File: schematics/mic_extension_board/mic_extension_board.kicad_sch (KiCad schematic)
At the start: 75 parts, among them J1 XLR3, J10 Conn_01x01_Male, J2 Conn_01x02_Male, J3 Aux In, J4 I2C Bus, J5 6Pin ISP, J6 Input/Output, J7 XLR3, J8 XLR3, J9 Conn_01x03_Female, SW1 Stompbutton 1, SW2 Stompbutton 2, SW3 Stompbutton 3, U1 TL074, U10 LM4881M/NOPB, U2 TL072, U3 APE8865N-33-HF-3, U4 NE5534, U5 ATmega88A-A, U6 24LC128, U7 MC78M05_TO252, U8 MC79M08_TO252

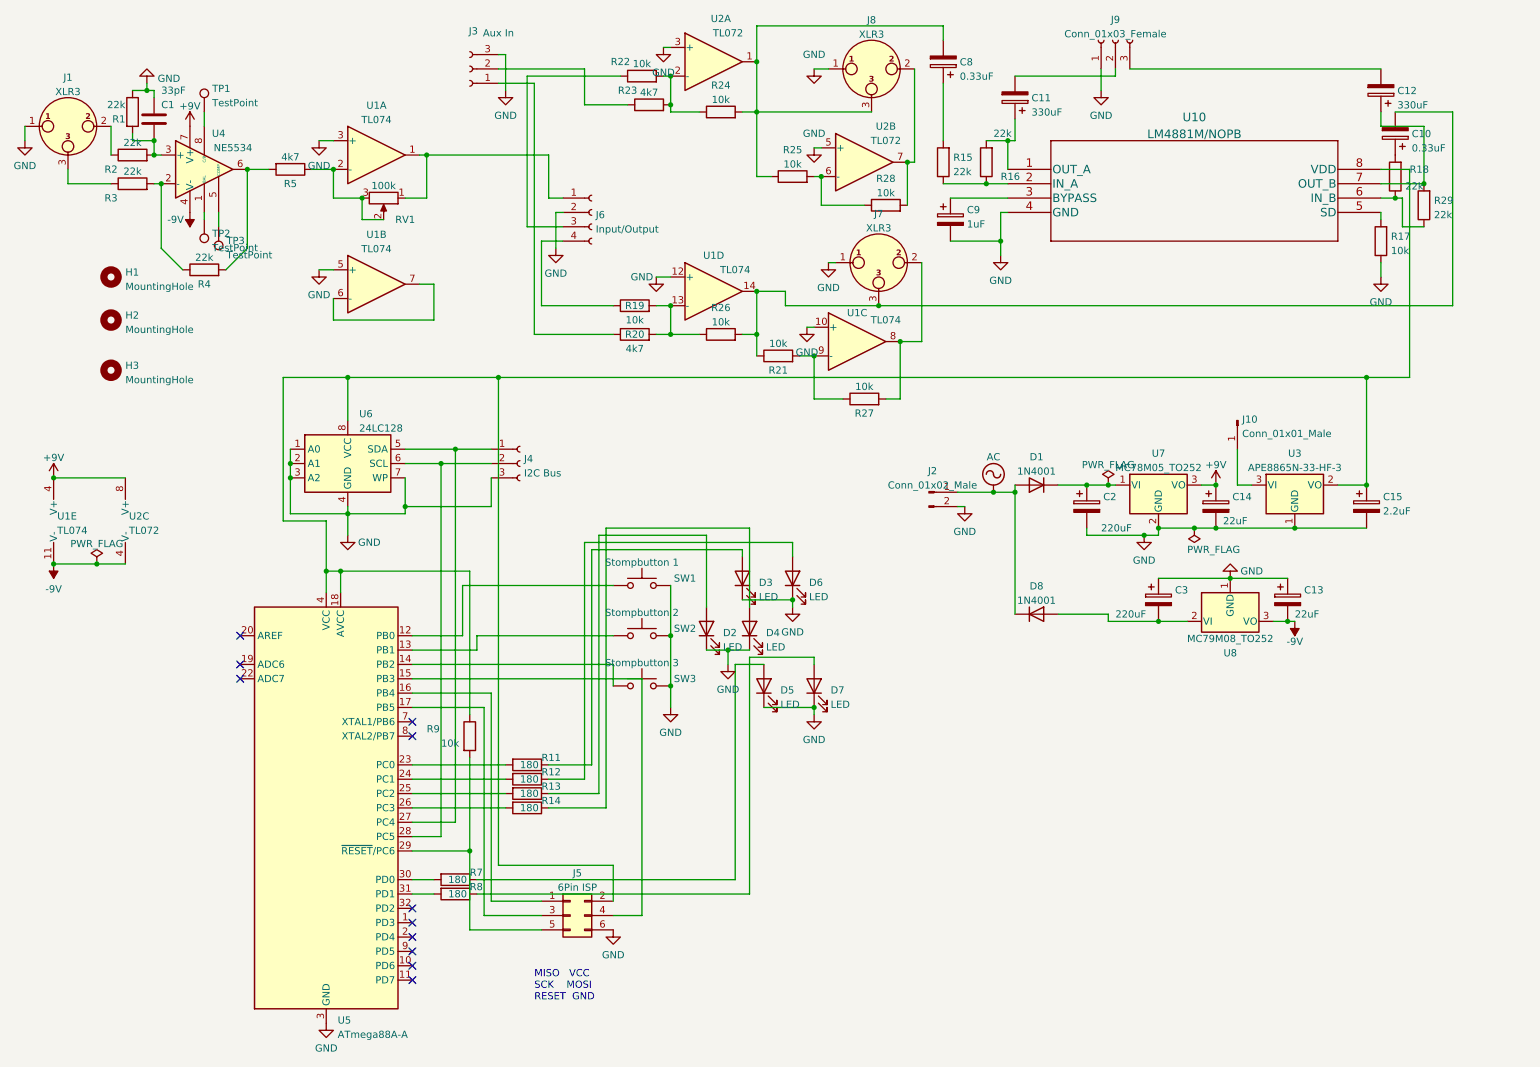
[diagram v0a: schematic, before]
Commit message: modified extension board schematic
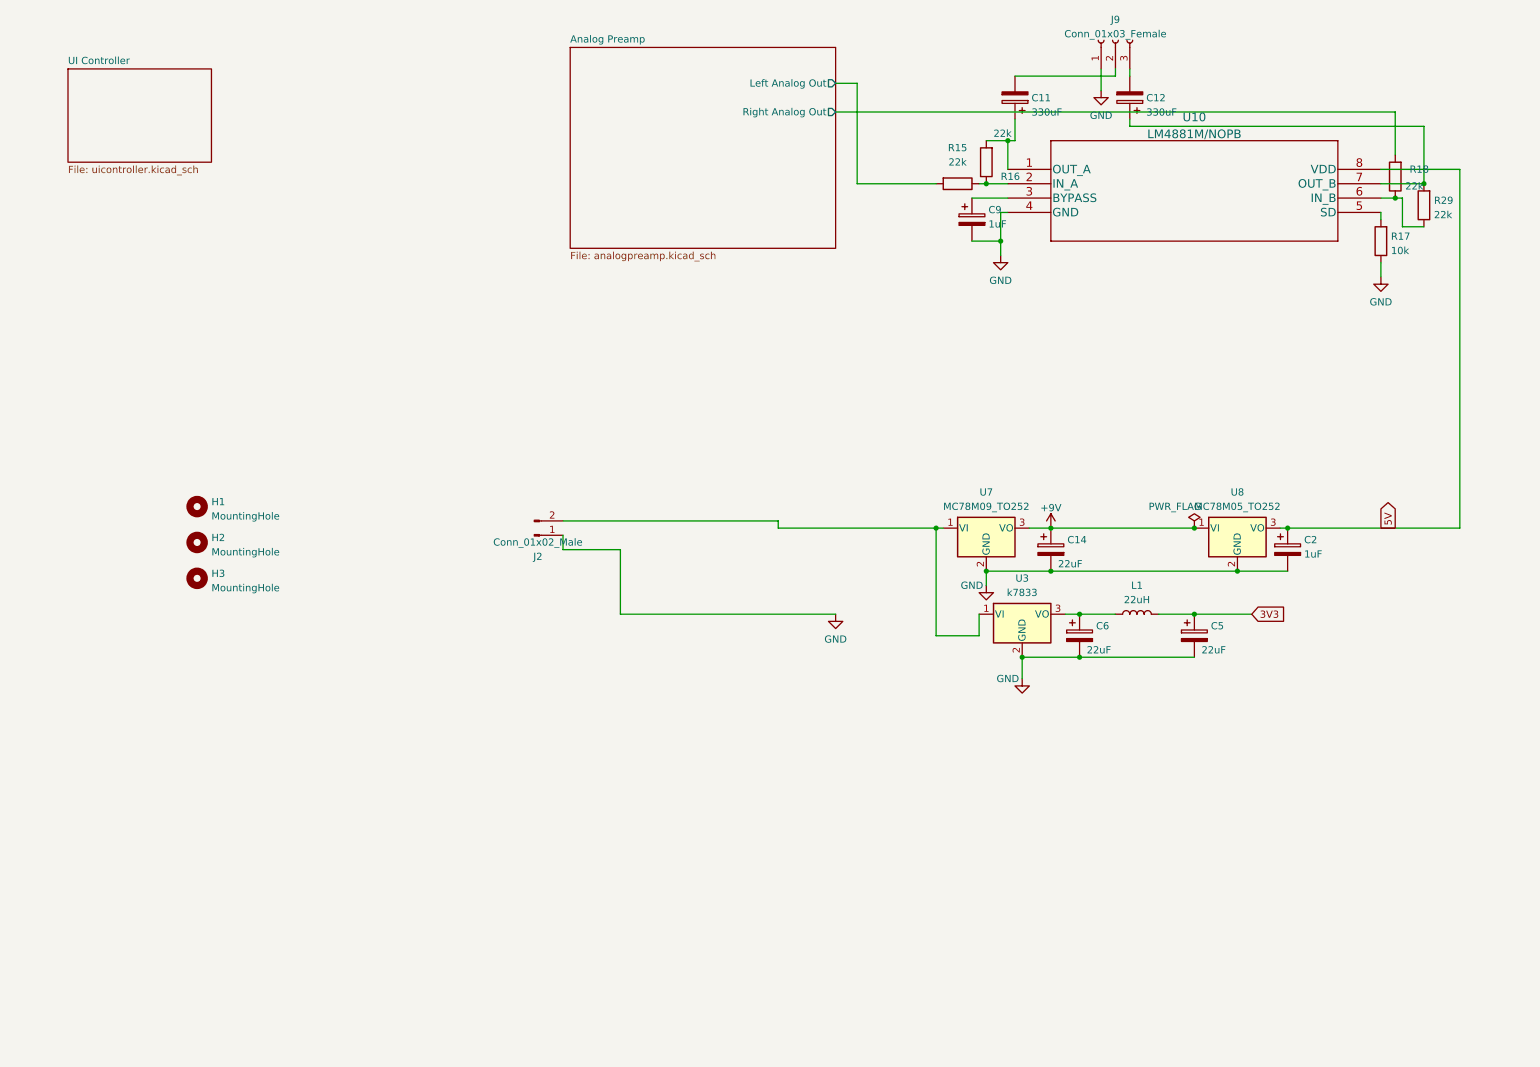
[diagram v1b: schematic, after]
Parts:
- removed C1: 33pF, Capacitor_SMD:C_0603_1608Metric_Pad1.08x0.95mm_HandSolder, symbol Device:C
- removed C10, C8: 0.33uF, Capacitor_SMD:CP_Elec_4x4.5, symbol Device:C_Polarized
- removed C13: 22uF, Capacitor_SMD:CP_Elec_4x4.5, symbol Device:C_Polarized
- removed C15: 2.2uF, Capacitor_SMD:CP_Elec_4x4.5, symbol Device:C_Polarized
- removed C3: 220uF, Capacitor_SMD:CP_Elec_6.3x7.7, symbol Device:C_Polarized
- removed D1, D8: 1N4001, Diode_THT:D_DO-41_SOD81_P10.16mm_Horizontal, symbol Diode:1N4001
- removed D2, D3, D4, D5, D6, D7: LED, Connector_PinHeader_2.54mm:PinHeader_1x02_P2.54mm_Vertical, symbol Device:LED
- removed J1, J7, J8: XLR3, Connector_PinHeader_2.54mm:PinHeader_1x03_P2.54mm_Vertical, symbol Connector:XLR3
- removed J10: Conn_01x01_Male, Connector_PinHeader_2.54mm:PinHeader_1x01_P2.54mm_Vertical, symbol Connector:Conn_01x01_Male
- removed J3: Aux In, Connector_PinHeader_2.54mm:PinHeader_1x03_P2.54mm_Vertical, symbol Connector:Conn_01x03_Female
- removed J4: I2C Bus, Connector_PinHeader_2.54mm:PinHeader_1x03_P2.54mm_Vertical, symbol Connector:Conn_01x03_Female
- removed J5: 6Pin ISP, Connector_PinHeader_2.54mm:PinHeader_2x03_P2.54mm_Vertical, symbol Connector_Generic:Conn_02x03_Odd_Even
- removed J6: Input/Output, Connector_PinHeader_2.54mm:PinHeader_1x04_P2.54mm_Vertical, symbol Connector:Conn_01x04_Female
- removed R1, R2, R3, R4: 22k, Resistor_SMD:R_0603_1608Metric_Pad0.98x0.95mm_HandSolder, symbol Device:R
- removed R11, R12, R13, R14, R7, R8: 180, Resistor_SMD:R_0603_1608Metric_Pad0.98x0.95mm_HandSolder, symbol Device:R
- removed R19, R21, R22, R24, R25, R26, R27, R28, R9: 10k, Resistor_SMD:R_0603_1608Metric_Pad0.98x0.95mm_HandSolder, symbol Device:R
- removed R20, R23, R5: 4k7, Resistor_SMD:R_0603_1608Metric_Pad0.98x0.95mm_HandSolder, symbol Device:R
- removed RV1: 100k, Connector_PinHeader_2.54mm:PinHeader_1x03_P2.54mm_Vertical, symbol Device:R_Potentiometer
- removed SW1: Stompbutton 1, Connector_PinHeader_2.54mm:PinHeader_1x02_P2.54mm_Vertical, symbol Switch:SW_Push
- removed SW2: Stompbutton 2, Connector_PinHeader_2.54mm:PinHeader_1x02_P2.54mm_Vertical, symbol Switch:SW_Push
- removed SW3: Stompbutton 3, Connector_PinHeader_2.54mm:PinHeader_1x02_P2.54mm_Vertical, symbol Switch:SW_Push
- removed TP1, TP2, TP3: TestPoint, TestPoint:TestPoint_Pad_D1.5mm, symbol Connector:TestPoint
- removed U1: TL074, Package_SO:SOIC-14_3.9x8.7mm_P1.27mm, symbol Amplifier_Operational:TL074
- removed U2: TL072, Package_SO:SOIC-8_3.9x4.9mm_P1.27mm, symbol Amplifier_Operational:TL072
- removed U3: APE8865N-33-HF-3, Package_TO_SOT_SMD:SOT-23, symbol Regulator_Linear:APE8865N-33-HF-3
- removed U4: NE5534, Package_SO:SOIC-8_3.9x4.9mm_P1.27mm, symbol Amplifier_Operational:NE5534
- removed U5: ATmega88A-A, Package_QFP:TQFP-32_7x7mm_P0.8mm, symbol MCU_Microchip_ATmega:ATmega88A-A
- removed U6: 24LC128, Package_SO:SOIC-8_3.9x4.9mm_P1.27mm, symbol Memory_EEPROM:24LC128
- removed U8: MC79M08_TO252, Package_TO_SOT_SMD:TO-252-2, symbol Regulator_Linear:MC79M08_TO252
- added C5, C6: 22uF, Capacitor_SMD:CP_Elec_4x4.5, symbol Device:C_Polarized
- added L1: 22uH, Inductor_SMD:L_0603_1608Metric_Pad1.05x0.95mm_HandSolder, symbol Device:L
- added U3: k7833, Connector_PinHeader_2.54mm:PinHeader_1x03_P2.54mm_Vertical, symbol Regulator_Linear:LM7809_TO220
- added U8: MC78M05_TO252, Package_TO_SOT_SMD:TO-252-2, symbol Regulator_Linear:MC78M05_TO252
- C2: value 220uF -> 1uF; footprint Capacitor_SMD:CP_Elec_6.3x7.7 -> Capacitor_SMD:CP_Elec_4x4.5
- U7: value MC78M05_TO252 -> MC78M09_TO252
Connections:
- net AC is gone; now on net GND: J2.1 (Pin_1)
- net +9V: now also U8.1 (VI)
- net GND: now also C5.2, C6.2, U3.2 (GND), U8.2 (GND); no longer J2.2 (Pin_2)
- net Analog Preamp/Right Analog Out: now reaches R18.2
- net 5V: now reaches U10.8 (VDD)
- net 5V: now also C2.1, U8.3 (VO)
- net at U7.1 (VI): now also J2.2 (Pin_2), U3.1 (VI); no longer C2.1
- net Analog Preamp/Left Analog Out: now reaches R15.2
- new net: C6.1, L1.1, U3.3 (VO)
- new net 3V3: C5.1, L1.2
- no-connect marks 11 -> 0
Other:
- added sheet Analog Preamp (analogpreamp.kicad_sch)
- added sheet UI Controller (uicontroller.kicad_sch)
- note removed: "MISO VCC SCK MOSI RESET GND"
- moved on the sheet: C12, C14, C9, H1, H2, H3, J2, R15, U7

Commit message: more layouting
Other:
- added sheet Codec (codec.kicad_sch)
- sheet Analog Preamp ports: added DacL, DacR, HiZ, Mic; removed none
- sheet UI Controller ports: added SCL, SDA; removed none
- moved on the sheet: C14, C2, C5, C6, J2, L1, U3, U7, U8

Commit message: finished full board
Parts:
- removed C11, C12: 330uF, Capacitor_SMD:CP_Elec_6.3x7.7, symbol Device:C_Polarized
- removed C9: 1uF, Capacitor_SMD:CP_Elec_4x4.5, symbol Device:C_Polarized
- removed J9: Conn_01x03_Female, Connector_PinHeader_2.54mm:PinHeader_1x03_P2.54mm_Vertical, symbol Connector:Conn_01x03_Female
- removed R15, R16, R18, R29: 22k, Resistor_SMD:R_0603_1608Metric_Pad0.98x0.95mm_HandSolder, symbol Device:R
- removed R17: 10k, Resistor_SMD:R_0603_1608Metric_Pad0.98x0.95mm_HandSolder, symbol Device:R
- removed U10: LM4881M/NOPB, Package_SO:SOIC-8_3.9x4.9mm_P1.27mm, symbol 2023-02-24_23-31-36:LM4881M/NOPB
- added C38, C39: C, Capacitor_SMD:C_0805_2012Metric_Pad1.18x1.45mm_HandSolder, symbol Device:C
- added D1, D8: LED, Connector_PinHeader_2.54mm:PinHeader_1x02_P2.54mm_Vertical, symbol Device:LED
- added J9: Conn_01x03, Connector_PinHeader_2.54mm:PinHeader_1x03_P2.54mm_Vertical, symbol Connector_Generic:Conn_01x03
- added R50, R51, R52, R53: R, Resistor_SMD:R_0603_1608Metric_Pad0.98x0.95mm_HandSolder, symbol Device:R
- added R54, R55: 180, Resistor_SMD:R_0603_1608Metric_Pad0.98x0.95mm_HandSolder, symbol Device:R
- added RV3, RV4, RV5: 25k, Connector_PinHeader_2.54mm:PinHeader_1x03_P2.54mm_Vertical, symbol Device:R_Potentiometer
- added SW4: Enter, Connector_PinHeader_2.54mm:PinHeader_1x02_P2.54mm_Vertical, symbol Switch:SW_Push
- added SW5: Exit, Connector_PinHeader_2.54mm:PinHeader_1x02_P2.54mm_Vertical, symbol Switch:SW_Push
- added U12: 128X64 OLED Display, Connector_PinHeader_2.54mm:PinHeader_1x07_P2.54mm_Vertical, symbol GraphicDisplay:128X64_OLED_Display
- added U13: Debug Port, Connector_PinHeader_2.54mm:PinHeader_1x06_P2.54mm_Vertical, symbol GraphicDisplay:DebugPort
- added U2: Pico, MCU_RaspberryPi_and_Boards:RPi_Pico_SMD_TH, symbol Raspberry Pi Pico:Pico
- C14, C5, C6: value 22uF -> C_Polarized
- C2: value 1uF -> C_Polarized
- L1: value 22uH -> L
- U3: value k7833 -> LM7809_TO220; footprint Connector_PinHeader_2.54mm:PinHeader_1x03_P2.54mm_Vertical -> Package_TO_SOT_THT:TO-220-3_Vertical
- U7: value MC78M09_TO252 -> MC78M05_TO252
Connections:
- net 5V: now also U13.3 (5V), U2.39 (VSYS)
- net Codec/SCL: now also U2.7 (GPIO5)
- net Codec/SDA: now also U2.6 (GPIO4)
- net Codec/codec_lrckl: now also U2.14 (GPIO10)
- net Codec/codec_reset: now also U2.5 (GPIO3)
- net Codec/codec_sclk: now also U2.15 (GPIO11)
- net Codec/codec_sdin: now also U2.16 (GPIO12)
- net Codec/codec_sdout: now also U2.12 (GPIO9)
- net GND: now also C38.2, C39.2, J9.2 (Pin_2), RV3.1, RV4.1, RV5.1, SW4.2, SW5.2, U12.7 (Ground), U13.4 (Ground), U2.13 (GND), U2.18 (GND), U2.23 (GND), U2.28 (GND), U2.3 (GND), U2.33 (AGND), U2.38 (GND), U2.42 (GND), U2.8 (GND)
- new net: U13.1 (UartTX), U2.1 (GPIO0)
- new net: C38.1, R51.2, U2.10 (GPIO7)
- new net: U12.1 (DC), U2.19 (GPIO14)
- new net: U13.2 (UartRX), U2.2 (GPIO1)
- new net: U12.5 (Reset), U2.20 (GPIO15)
- new net: D8.1 (K), U2.21 (GPIO16)
- new net: D1.1 (K), U2.22 (GPIO17)
- new net: U12.3 (SCLK), U2.24 (GPIO18)
- new net: U12.2 (Data), U2.25 (GPIO19)
- new net: SW5.1, U2.26 (GPIO20)
- new net: U12.4 (CS), U2.27 (GPIO21)
- new net: SW4.1, U2.29 (GPIO22)
- new net: RV3.2, U2.31 (GPIO26_ADC0)
- new net: RV4.2, U2.32 (GPIO27_ADC1)
- new net: RV5.2, U2.34 (GPIO28_ADC2)
- new net: R50.1, R52.1, R54.2, R55.2, RV3.3, RV4.3, RV5.3, U12.6 (3.3V), U2.36 (3V3)
- new net: U13.6 (SWCLK), U2.41 (SWCLK)
- new net: U13.5 (SWDIO), U2.43 (SWDIO)
- new net: C39.1, R53.2, U2.9 (GPIO6)
- new net: J9.3 (Pin_3), R50.2, R51.1
- new net: D8.2 (A), R55.1
- new net: J9.1 (Pin_1), R52.2, R53.1
- new net: D1.2 (A), R54.1
- no-connect marks 0 -> 7
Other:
- added sheet Headphone Amp (untitled.kicad_sch)
- moved on the sheet: C14, C2, C5, C6, H1, H2, H3, J2, L1, U3, U7, U8

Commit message: re-added component values previously lost due to kicad mishap
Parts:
- C14, C5, C6: value C_Polarized -> 22uF
- C2: value C_Polarized -> 1uF
- C38, C39: value C -> 0.01uF
- L1: value L -> 22uH
- R50, R51, R52, R53: value R -> 10k
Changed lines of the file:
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@@
       (effects (font (size 1.27 1.27)) (justify left))
     )
-    (property "Value" "R" (at 63.5 111.76 0)
+    (property "Value" "10k" (at 63.5 111.76 0)
       (effects (font (size 1.27 1.27)) (justify left))
     )
@@
       (effects (font (size 1.27 1.27)) (justify left))
     )
-    (property "Value" "C" (at 55.88 149.86 0)
+    (property "Value" "0.01uF" (at 55.88 149.86 0)
       (effects (font (size 1.27 1.27)) (justify left))
     )
@@
       (effects (font (size 1.27 1.27)) (justify left))
     )
-    (property "Value" "R" (at 54.61 133.35 0)
+    (property "Value" "10k" (at 54.61 133.35 0)
       (effects (font (size 1.27 1.27)) (justify left))
     )
@@
       (effects (font (size 1.27 1.27)))
     )
-    (property "Value" "L" (at 252.73 85.09 90)
+    (property "Value" "22uH" (at 252.73 85.09 90)
       (effects (font (size 1.27 1.27)))
     )
@@
       (effects (font (size 1.27 1.27)) (justify left))
     )
-    (property "Value" "C" (at 62.23 120.65 0)
+    (property "Value" "0.01uF" (at 62.23 120.65 0)
       (effects (font (size 1.27 1.27)) (justify left))
     )
@@
       (effects (font (size 1.27 1.27)) (justify left))
     )
-    (property "Value" "R" (at 54.61 142.24 0)
+    (property "Value" "10k" (at 54.61 142.24 0)
       (effects (font (size 1.27 1.27)) (justify left))
     )
@@
       (effects (font (size 1.27 1.27)) (justify left))
     )
-    (property "Value" "C_Polarized" (at 238.76 78.74 0)
+    (property "Value" "22uF" (at 238.76 78.74 0)
       (effects (font (size 1.27 1.27)) (justify left))
     )
@@
       (effects (font (size 1.27 1.27)) (justify left))
     )
-    (property "Value" "C_Polarized" (at 264.16 93.98 0)
+    (property "Value" "22uF" (at 264.16 93.98 0)
       (effects (font (size 1.27 1.27)) (justify left))
     )
@@
       (effects (font (size 1.27 1.27)) (justify left))
     )
-    (property "Value" "R" (at 60.96 104.14 0)
+    (property "Value" "10k" (at 60.96 104.14 0)
       (effects (font (size 1.27 1.27)) (justify left))
     )
@@
   (symbol (lib_id "Device:C_Polarized") (at 260.35 76.2 0) (unit 1)
     (in_bom yes) (on_board yes) (dnp no) (fields_autoplaced)
-    (property "Reference" "C2" (at 263.271 74.4763 0)
-      (effects (font (size 1.27 1.27)) (justify left))
-    )
-    (property "Value" "C_Polarized" (at 263.271 77.0132 0)
+    (property "Reference" "C2" (at 264.16 74.041 0)
+      (effects (font (size 1.27 1.27)) (justify left))
+    )
+    (property "Value" "1uF" (at 264.16 76.581 0)
       (effects (font (size 1.27 1.27)) (justify left))
     )
@@
       (effects (font (size 1.27 1.27)) (justify left))
     )
-    (property "Value" "C_Polarized" (at 243.84 93.98 0)
-      (effects (font (size 1.27 1.27)) (justify left))
-    )
+    (property "Value" "22uF" (at 243.84 93.98 0)
+      (effects (font (size 1.27 1.27)) (justify left))
+    )

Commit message: schematic / pcb update
* digital part is now driven from 3.3v only
* 3.3v switching supply is now present as discrete parts
* top copper fill is 3.3v
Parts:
- removed U3: LM7809_TO220, Package_TO_SOT_THT:TO-220-3_Vertical, symbol Regulator_Linear:LM7809_TO220
- added C40: 0.1uF, Capacitor_SMD:C_1210_3225Metric_Pad1.33x2.70mm_HandSolder, symbol Device:C
- added R56: 10k, Resistor_SMD:R_0603_1608Metric_Pad0.98x0.95mm_HandSolder, symbol Device:R
- added U14: AP63203WU, Package_TO_SOT_SMD:TSOT-23-6, symbol Regulator_Switching:AP63203WU
- C6: value 22uF -> 10uF
- L1: value 22uH -> 3.9uH; footprint Inductor_SMD:L_0603_1608Metric_Pad1.05x0.95mm_HandSolder -> Inductor_SMD:L_1812_4532Metric_Pad1.30x3.40mm_HandSolder
- renumbered RV3 to P0, RV4 to P1, RV5 to P2
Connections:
- net 3V3: now also U13.3 (Vsys), U2.39 (VSYS), U14.1 (FB)
- net 5V: no longer U13.3 (5V), U2.39 (VSYS)
- net GND: now also U14.4 (GND)
- net at U12.5 (Reset), U2.20 (GPIO15): now also R56.1
- net at P0.3, P1.3, P2.3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: now also R56.2
- net at L1.1: now also C40.2, U14.5 (SW); no longer C6.1
- net at J2.2 (Pin_2), U7.1 (VI): now also C6.1, U14.2 (EN), U14.3 (IN)
- new net: C40.1, U14.6 (BST)
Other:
- moved on the sheet: C6, L1

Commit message: schematics
adjusted track widths
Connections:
- net Vin: now reaches C6.1, J2.2 (Pin_2), U14.2 (EN), U14.3 (IN), U7.1 (VI)
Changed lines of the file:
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@@
+    )
+  )
+  (global_label "Vin" (shape input) (at 208.28 72.39 90) (fields_autoplaced)
+    (effects (font (size 1.27 1.27)) (justify left))
+    (property "Intersheetrefs" "${INTERSHEET_REFS}" (at 208.28 66.5624 90)
+      (effects (font (size 1.27 1.27)) (justify left) hide)
     )
   )

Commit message: pcb: layout changes, c headers: documentation
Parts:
- removed U8: MC78M05_TO252, Package_TO_SOT_SMD:TO-252-2, symbol Regulator_Linear:MC78M05_TO252
- added U3: LM1117DT-5.0, Package_TO_SOT_SMD:TO-252-3_TabPin2, symbol Regulator_Linear:LM1117DT-5.0
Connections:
- net +9V: now also U3.3 (VI)
- net 5V: now also U3.2 (VO)
- net GND: now also U3.1 (GND)
